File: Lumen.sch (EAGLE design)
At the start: 25 parts, among them J1 AVR_SPI_PRG_6PTH, U1 Tiny45-20-SMT, Y1 8MHZ

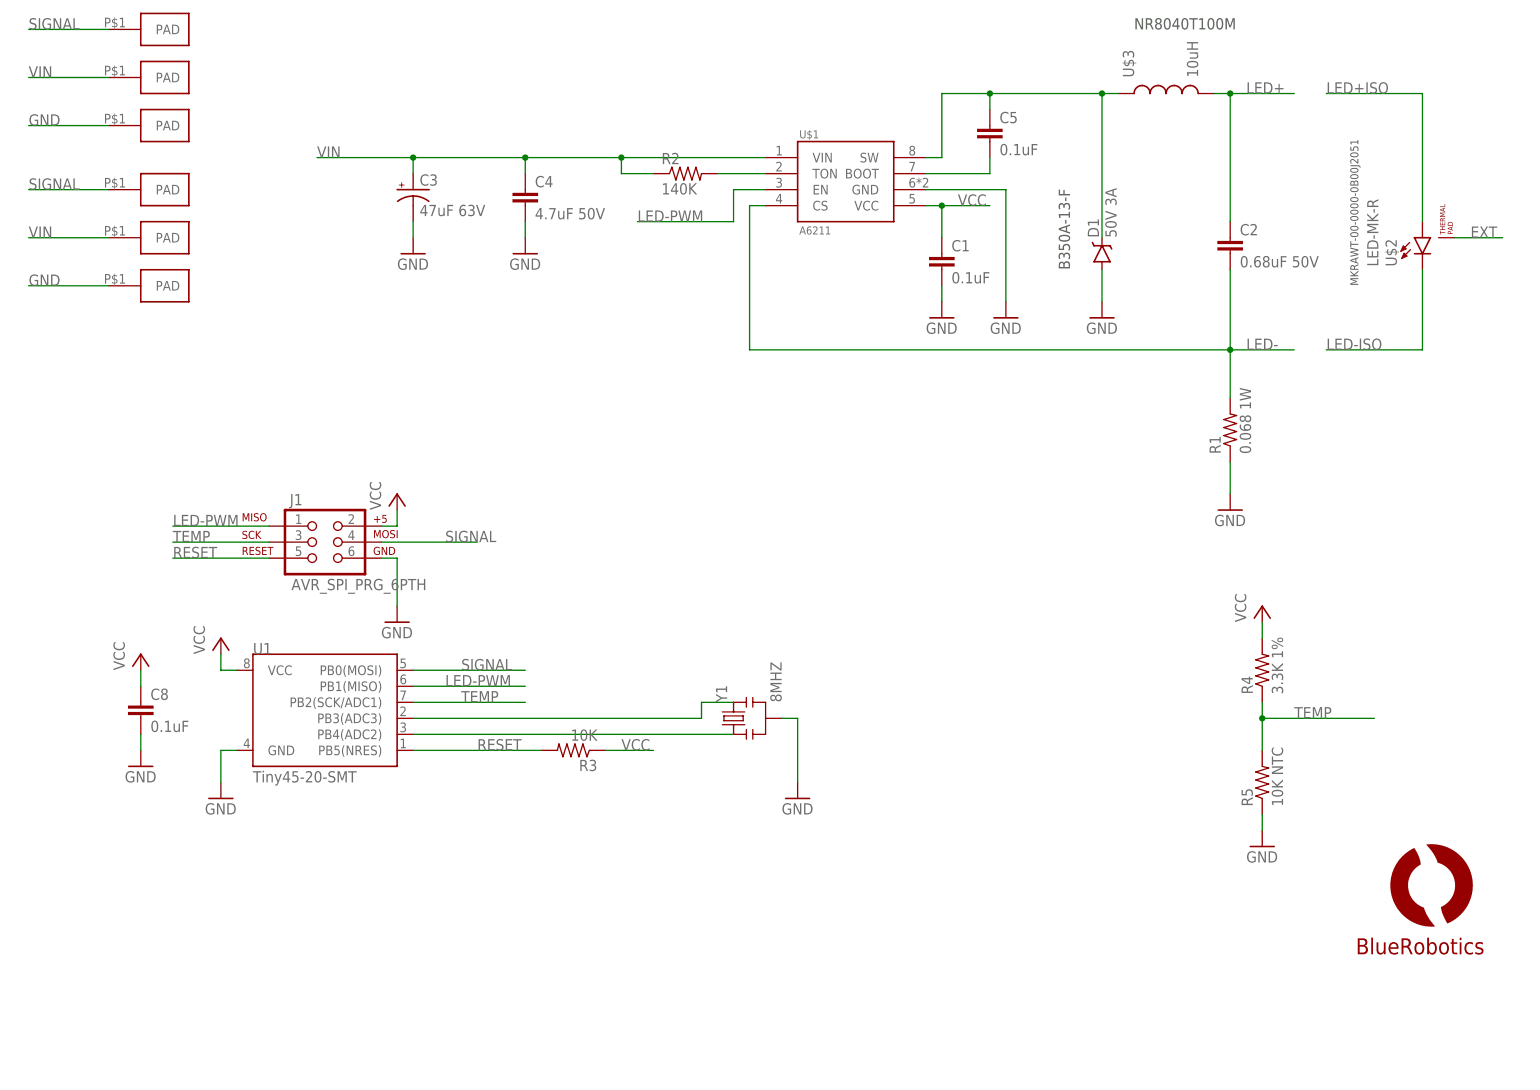
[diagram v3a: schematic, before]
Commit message: Fixed a lot of little things. Added regulator back into the design. Upgrade capacitor voltage ratings.
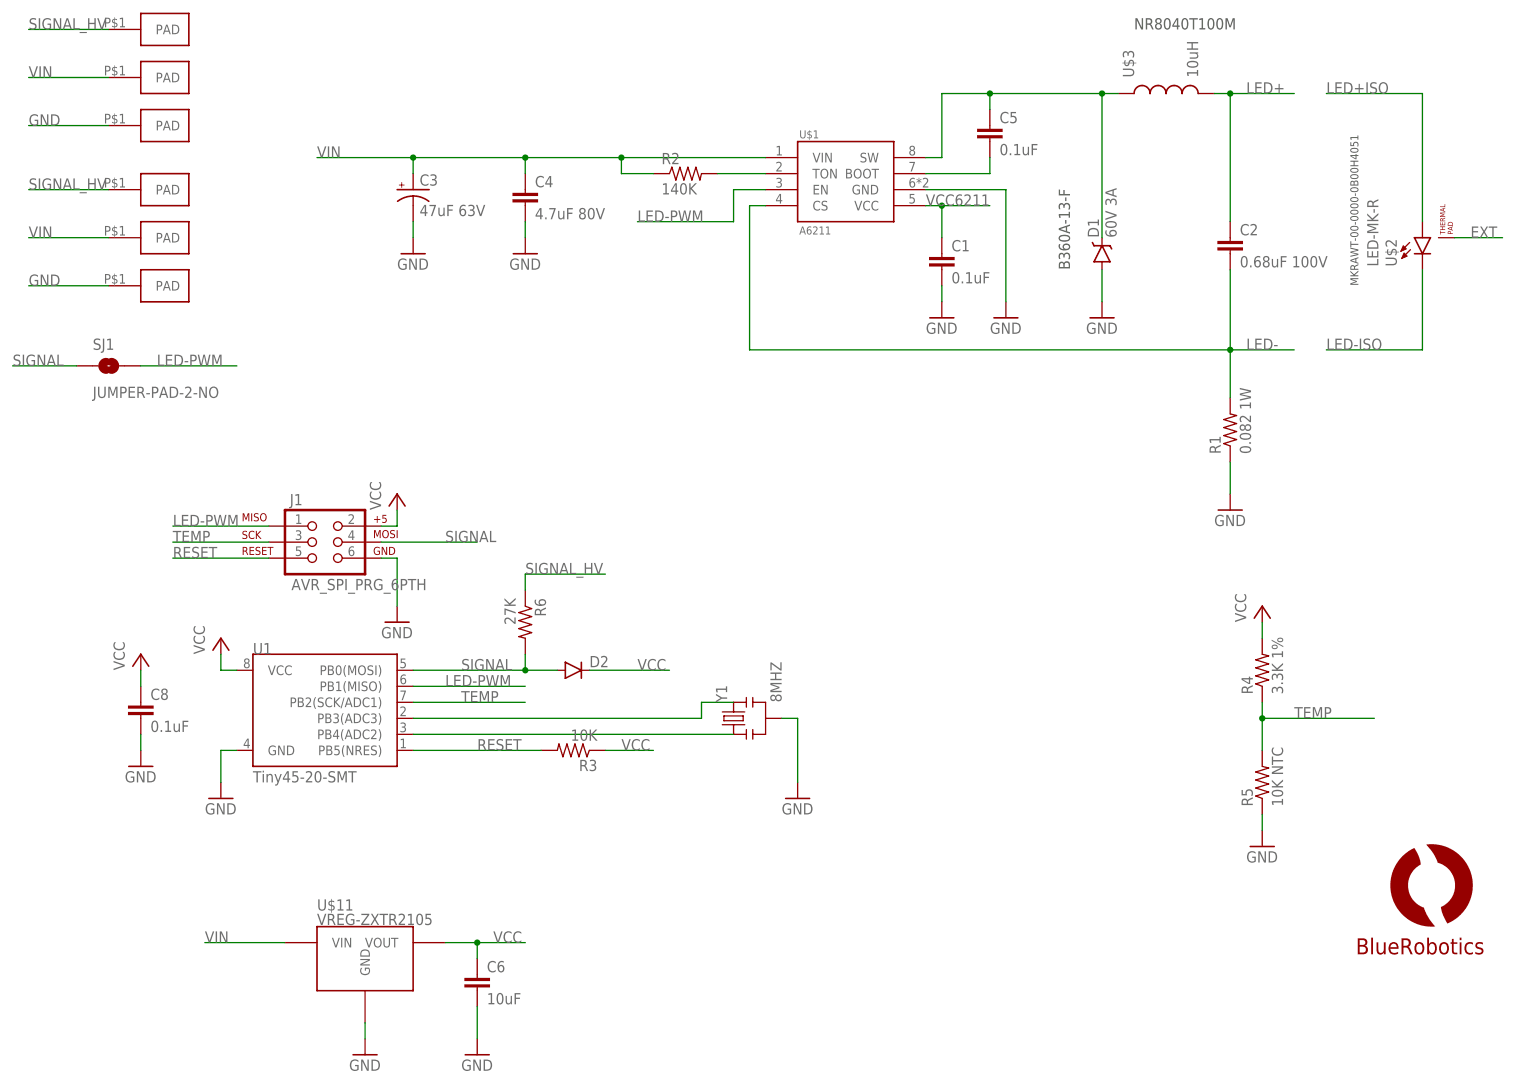
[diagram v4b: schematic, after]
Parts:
- added C6: 10uF, resistor:C-EUC0603
- added D2: (no value), SparkFun-DiscreteSemi:DIODESOD523
- added R6: 27K, resistor:R-US_R0603
- added SJ1: JUMPER-PAD-2-NO, SparkFun-Passives:JUMPER-PAD-2-NO
- added U$11: VREG-ZXTR2105, BlueRobotics-Main:VREG-ZXTR2105
- C2: value 0.68uF 50V -> 0.68uF 100V
- C4: value 4.7uF 50V -> 4.7uF 80V; device resistor:C-EUC1206 -> resistor:C-EUC1210
- D1: value 50V 3A -> 60V 3A
- R1: value 0.068 1W -> 0.082 1W; device resistor:R-US_R1210 -> resistor:R-US_R2512
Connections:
- new net SIGNAL_HV: R6.1, U$4.PAD, U$7.PAD
- new net VCC6211: C1.1, U$1.VCC
- net GND: now also C6.2, U$11.GND
- net LED-PWM: now also SJ1.2
- net SIGNAL: now also D2.A, R6.2, SJ1.1; no longer U$4.PAD, U$7.PAD
- net VCC: now also C6.1, D2.C, U$11.VOUT; no longer C1.1, U$1.VCC
- net VIN: now also U$11.VIN
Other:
- note added: "B360A-13-F"
- note added: "MKRAWT-00-0000-0B00H4051"
- note removed: "B350A-13-F"
- note removed: "MKRAWT-00-0000-0B00J2051"
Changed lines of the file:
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@@
 <part name="C3" library="SparkFun-Capacitors" deviceset="CAP_POL" device="PTH1" value="47uF 63V"/>
 <part name="U$3" library="BlueRobotics-Main" deviceset="INDUCTOR" device="8040" value="10uH"/>
-<part name="D1" library="SparkFun-DiscreteSemi" deviceset="DIODE-SCHOTTKY" device="-B340A" value="50V 3A"/>
-<part name="R1" library="resistor" deviceset="R-US_" device="R1210" value="0.068 1W"/>
-<part name="C4" library="resistor" deviceset="C-EU" device="C1206" value="4.7uF 50V"/>
-<part name="C2" library="resistor" deviceset="C-EU" device="C0805" value="0.68uF 50V"/>
+<part name="D1" library="SparkFun-DiscreteSemi" deviceset="DIODE-SCHOTTKY" device="-B340A" value="60V 3A"/>
+<part name="R1" library="resistor" deviceset="R-US_" device="R2512" value="0.082 1W"/>
+<part name="C4" library="resistor" deviceset="C-EU" device="C1210" value="4.7uF 80V"/>
+<part name="C2" library="resistor" deviceset="C-EU" device="C0805" value="0.68uF 100V"/>
 <part name="C1" library="resistor" deviceset="C-EU" device="C0603" value="0.1uF"/>
 <part name="C5" library="resistor" deviceset="C-EU" device="C0603" value="0.1uF"/>
@@
 <part name="GND8" library="supply1" deviceset="GND" device=""/>
 <part name="U$10" library="BlueRobotics-Main" deviceset="LOGO" device="BR-LOGO-MS" value="LOGOBR-LOGO-MS"/>
+<part name="U$11" library="BlueRobotics-Main" deviceset="VREG-ZXTR2105" device=""/>
+<part name="GND11" library="supply1" deviceset="GND" device=""/>
+<part name="C6" library="resistor" deviceset="C-EU" device="C0603" value="10uF"/>
+<part name="GND13" library="supply1" deviceset="GND" device=""/>
+<part name="SJ1" library="SparkFun-Passives" deviceset="JUMPER-PAD-2-NO" device=""/>
+<part name="D2" library="SparkFun-DiscreteSemi" deviceset="DIODE" device="SOD523"/>
+<part name="R6" library="resistor" deviceset="R-US_" device="R0603" value="27K"/>
 </parts>
 <sheets>
@@
 <plain>
 <text x="185.42" y="175.26" size="1.778" layer="97">NR8040T100M</text>
-<text x="175.26" y="137.16" size="1.778" layer="97" rot="R90">B350A-13-F</text>
-<text x="220.98" y="134.62" size="1.27" layer="97" rot="R90">MKRAWT-00-0000-0B00J2051</text>
+<text x="175.26" y="137.16" size="1.778" layer="97" rot="R90">B360A-13-F</text>
+<text x="220.98" y="134.62" size="1.27" layer="97" rot="R90">MKRAWT-00-0000-0B00H4051</text>
 </plain>
 <instances>
@@
 <instance part="GND8" gate="1" x="132.08" y="53.34"/>
 <instance part="U$10" gate="G$1" x="226.06" y="33.02"/>
+<instance part="U$11" gate="G$1" x="63.5" y="25.4"/>
+<instance part="GND11" gate="1" x="63.5" y="12.7"/>
+<instance part="C6" gate="G$1" x="81.28" y="25.4"/>
+<instance part="GND13" gate="1" x="81.28" y="12.7"/>
+<instance part="SJ1" gate="G$1" x="22.86" y="121.92"/>
+<instance part="D2" gate="G$1" x="96.52" y="73.66"/>
+<instance part="R6" gate="G$1" x="88.9" y="81.28" rot="R270"/>
 </instances>
 <busses>
@@
 <pinref part="Y1" gate="G$1" pin="2"/>
 <wire x1="132.08" y1="66.04" x2="129.54" y2="66.04" width="0.1524" layer="91"/>
+</segment>
+<segment>
+<pinref part="GND11" gate="1" pin="GND"/>
+<pinref part="U$11" gate="G$1" pin="GND"/>
+<wire x1="63.5" y1="15.24" x2="63.5" y2="17.78" width="0.1524" layer="91"/>
+</segment>
+<segment>
+<pinref part="GND13" gate="1" pin="GND"/>
+<pinref part="C6" gate="G$1" pin="2"/>
+<wire x1="81.28" y1="15.24" x2="81.28" y2="20.32" width="0.1524" layer="91"/>
 </segment>
 </net>
@@
 <label x="10.16" y="142.24" size="1.778" layer="95"/>
 </segment>
+<segment>
+<pinref part="U$11" gate="G$1" pin="VIN"/>
+<wire x1="50.8" y1="30.48" x2="38.1" y2="30.48" width="0.1524" layer="91"/>
+<label x="38.1" y="30.48" size="1.778" layer="95"/>
+</segment>
 </net>
 <net name="LED-PWM" class="0">
@@
 <wire x1="48.26" y1="96.52" x2="33.02" y2="96.52" width="0.1524" layer="91"/>
 <label x="33.02" y="96.52" size="1.778" layer="95"/>
+</segment>
+<segment>
+<pinref part="SJ1" gate="G$1" pin="2"/>
+<wire x1="27.94" y1="121.92" x2="43.18" y2="121.92" width="0.1524" layer="91"/>
+<label x="30.48" y="121.92" size="1.778" layer="95"/>
 </segment>
 </net>
@@
 <net name="SIGNAL" class="0">
 <segment>
-<pinref part="U$4" gate="G$1" pin="PAD"/>
-<wire x1="22.86" y1="175.26" x2="10.16" y2="175.26" width="0.1524" layer="91"/>
-<label x="10.16" y="175.26" size="1.778" layer="95"/>
-</segment>
-<segment>
-<pinref part="U$7" gate="G$1" pin="PAD"/>
-<wire x1="22.86" y1="149.86" x2="10.16" y2="149.86" width="0.1524" layer="91"/>
-<label x="10.16" y="149.86" size="1.778" layer="95"/>
-</segment>
-<segment>
 <pinref part="U1" gate="G$1" pin="PB0(MOSI)"/>
 <wire x1="71.12" y1="73.66" x2="88.9" y2="73.66" width="0.1524" layer="91"/>
 <label x="78.74" y="73.66" size="1.778" layer="95"/>
+<pinref part="D2" gate="G$1" pin="A"/>
+<pinref part="R6" gate="G$1" pin="2"/>
+<wire x1="88.9" y1="73.66" x2="93.98" y2="73.66" width="0.1524" layer="91"/>
+<wire x1="88.9" y1="76.2" x2="88.9" y2="73.66" width="0.1524" layer="91"/>
+<junction x="88.9" y="73.66"/>
 </segment>
 <segment>
@@
 <wire x1="66.04" y1="93.98" x2="81.28" y2="93.98" width="0.1524" layer="91"/>
 <label x="76.2" y="93.98" size="1.778" layer="95"/>
+</segment>
+<segment>
+<pinref part="SJ1" gate="G$1" pin="1"/>
+<wire x1="17.78" y1="121.92" x2="7.62" y2="121.92" width="0.1524" layer="91"/>
+<label x="7.62" y="121.92" size="1.778" layer="95"/>
 </segment>
 </net>
@@
 </segment>
 <segment>
-<pinref part="C1" gate="G$1" pin="1"/>
-<wire x1="154.94" y1="142.24" x2="154.94" y2="147.32" width="0.1524" layer="91"/>
-<pinref part="U$1" gate="G$1" pin="VCC"/>
-<wire x1="154.94" y1="147.32" x2="152.4" y2="147.32" width="0.1524" layer="91"/>
-<wire x1="154.94" y1="147.32" x2="162.56" y2="147.32" width="0.1524" layer="91"/>
-<junction x="154.94" y="147.32"/>
-<label x="157.48" y="147.32" size="1.778" layer="95"/>
+<pinref part="U$11" gate="G$1" pin="VOUT"/>
+<wire x1="76.2" y1="30.48" x2="81.28" y2="30.48" width="0.1524" layer="91"/>
+<label x="83.82" y="30.48" size="1.778" layer="95"/>
+<pinref part="C6" gate="G$1" pin="1"/>
+<wire x1="81.28" y1="30.48" x2="88.9" y2="30.48" width="0.1524" layer="91"/>
+<wire x1="81.28" y1="27.94" x2="81.28" y2="30.48" width="0.1524" layer="91"/>
+<junction x="81.28" y="30.48"/>
+</segment>
+<segment>
+<pinref part="D2" gate="G$1" pin="C"/>
+<wire x1="99.06" y1="73.66" x2="111.76" y2="73.66" width="0.1524" layer="91"/>
+<label x="106.68" y="73.66" size="1.778" layer="95"/>
 </segment>
 </net>
@@
 </segment>
 </net>
+<net name="VCC6211" class="0">
+<segment>
+<pinref part="C1" gate="G$1" pin="1"/>
+<wire x1="154.94" y1="142.24" x2="154.94" y2="147.32" width="0.1524" layer="91"/>
+<pinref part="U$1" gate="G$1" pin="VCC"/>
+<wire x1="154.94" y1="147.32" x2="152.4" y2="147.32" width="0.1524" layer="91"/>
+<wire x1="154.94" y1="147.32" x2="162.56" y2="147.32" width="0.1524" layer="91"/>
+<junction x="154.94" y="147.32"/>
+<label x="152.4" y="147.32" size="1.778" layer="95"/>
+</segment>
+</net>
+<net name="SIGNAL_HV" class="0">
+<segment>
+<pinref part="R6" gate="G$1" pin="1"/>
+<wire x1="88.9" y1="86.36" x2="88.9" y2="88.9" width="0.1524" layer="91"/>
+<wire x1="88.9" y1="88.9" x2="101.6" y2="88.9" width="0.1524" layer="91"/>
+<label x="88.9" y="88.9" size="1.778" layer="95"/>
+</segment>
+<segment>
+<pinref part="U$7" gate="G$1" pin="PAD"/>
+<wire x1="22.86" y1="149.86" x2="10.16" y2="149.86" width="0.1524" layer="91"/>
+<label x="10.16" y="149.86" size="1.778" layer="95"/>
+</segment>
+<segment>
+<pinref part="U$4" gate="G$1" pin="PAD"/>
+<wire x1="22.86" y1="175.26" x2="10.16" y2="175.26" width="0.1524" layer="91"/>
+<label x="10.16" y="175.26" size="1.778" layer="95"/>
+</segment>
+</net>

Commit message: Fixed some layout issues per John's suggestion. Added pads for a snubber that will probably not be populated.
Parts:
- added C7: NP, resistor:C-EUC0603
- added R7: NP, resistor:R-US_R0603
- D1: device SparkFun-DiscreteSemi:DIODE-SCHOTTKY-B340A -> BlueRobotics-Main:DIODE-SCHOTTKYSMA
- D2: value (none) -> BAT54; device SparkFun-DiscreteSemi:DIODESOD523 -> BlueRobotics-Main:DIODE-SCHOTTKYSOD523
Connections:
- new net N$2: C7.2, R7.1
- net GND: now also R7.2
- net N$5: now also C7.1
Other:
- note added: "Snubber"
- moved on the sheet: C1, C3, C4, C5, R2, U$1

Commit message: More updates based on J.N. comments. Ready to order I believe.
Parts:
- R7: device resistor:R-US_R0603 -> resistor:R-US_R1206
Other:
- moved on the sheet: R4, R5
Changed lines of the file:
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@@
 <part name="U1" library="SparkFun-DigitalIC" deviceset="ATTINY45" device="TINY45-20-SMT" value="Tiny45-20-SMT"/>
 <part name="U$1" library="BlueRobotics-Main" deviceset="A6211" device=""/>
-<part name="FRAME1" library="BlueRobotics-Main" deviceset="FRAME-BLUEROBOTICS" device="" value="µC and LED Driver"/>
+<part name="FRAME1" library="BlueRobotics-Main" deviceset="FRAME-BLUEROBOTICS" device="" value="Microcontroller and LED Driver"/>
 <part name="U$2" library="BlueRobotics-Main" deviceset="LED-MK-R" device=""/>
 <part name="C3" library="SparkFun-Capacitors" deviceset="CAP_POL" device="PTH1" value="47uF 63V"/>
@@
 <part name="GND14" library="supply1" deviceset="GND" device=""/>
 <part name="C7" library="resistor" deviceset="C-EU" device="C0603" value="NP"/>
-<part name="R7" library="resistor" deviceset="R-US_" device="R0603" value="NP"/>
+<part name="R7" library="resistor" deviceset="R-US_" device="R1206" value="NP"/>
 </parts>
 <sheets>
@@
 <instance part="U$8" gate="G$1" x="33.02" y="142.24"/>
 <instance part="U$9" gate="G$1" x="33.02" y="134.62"/>
-<instance part="R4" gate="G$1" x="205.74" y="73.66" rot="R90"/>
-<instance part="R5" gate="G$1" x="205.74" y="55.88" rot="R90"/>
-<instance part="GND9" gate="1" x="205.74" y="45.72"/>
-<instance part="P+1" gate="VCC" x="205.74" y="83.82"/>
+<instance part="R4" gate="G$1" x="165.1" y="73.66" rot="R90"/>
+<instance part="R5" gate="G$1" x="165.1" y="55.88" rot="R90"/>
+<instance part="GND9" gate="1" x="165.1" y="45.72"/>
+<instance part="P+1" gate="VCC" x="165.1" y="83.82"/>
 <instance part="P+2" gate="VCC" x="40.64" y="78.74"/>
 <instance part="P+3" gate="VCC" x="68.58" y="101.6"/>
@@
 <pinref part="GND9" gate="1" pin="GND"/>
 <pinref part="R5" gate="G$1" pin="1"/>
-<wire x1="205.74" y1="48.26" x2="205.74" y2="50.8" width="0.1524" layer="91"/>
+<wire x1="165.1" y1="48.26" x2="165.1" y2="50.8" width="0.1524" layer="91"/>
 </segment>
 <segment>
@@
 <pinref part="R4" gate="G$1" pin="2"/>
 <pinref part="P+1" gate="VCC" pin="VCC"/>
-<wire x1="205.74" y1="78.74" x2="205.74" y2="81.28" width="0.1524" layer="91"/>
+<wire x1="165.1" y1="78.74" x2="165.1" y2="81.28" width="0.1524" layer="91"/>
 </segment>
 <segment>
@@
 <pinref part="R5" gate="G$1" pin="2"/>
 <pinref part="R4" gate="G$1" pin="1"/>
-<wire x1="205.74" y1="60.96" x2="205.74" y2="66.04" width="0.1524" layer="91"/>
-<wire x1="205.74" y1="66.04" x2="205.74" y2="68.58" width="0.1524" layer="91"/>
-<wire x1="205.74" y1="66.04" x2="223.52" y2="66.04" width="0.1524" layer="91"/>
-<junction x="205.74" y="66.04"/>
-<label x="210.82" y="66.04" size="1.778" layer="95"/>
-</segment>
-</net>
+<wire x1="165.1" y1="60.96" x2="165.1" y2="66.04" width="0.1524" layer="91"/>
+<wire x1="165.1" y1="66.04" x2="165.1" y2="68.58" width="0.1524" layer="91"/>
+<wire x1="165.1" y1="66.04" x2="182.88" y2="66.04" width="0.1524" layer="91"/>
+<junction x="165.1" y="66.04"/>
+<label x="170.18" y="66.04" size="1.778" layer="95"/>
+</segment>
+</net>

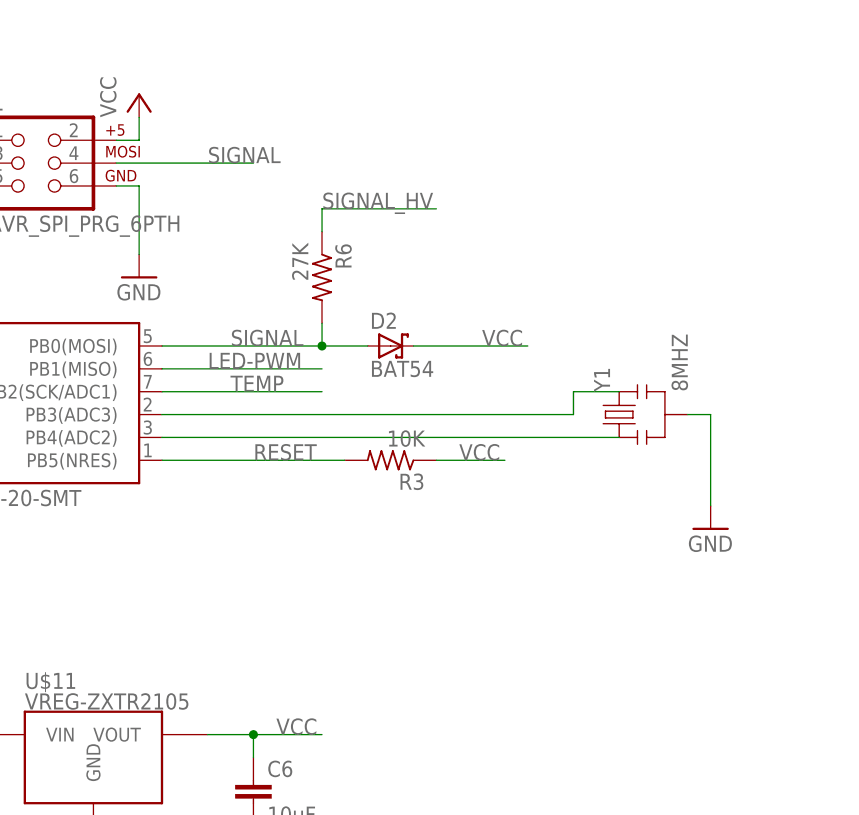
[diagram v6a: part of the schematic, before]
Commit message: Adjusted signal pull-down for 3.3V compatibility.
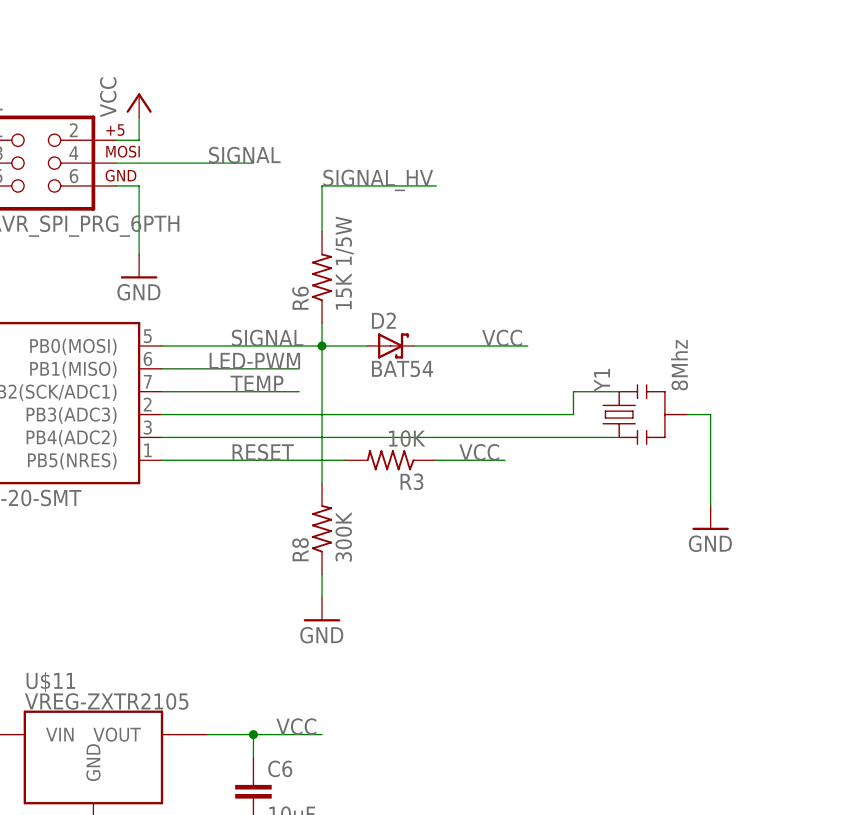
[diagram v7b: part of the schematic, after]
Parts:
- added R8: 300K, resistor:R-US_R0402
- R6: value 27K -> 15K 1/5W; device resistor:R-US_R0603 -> resistor:R-US_R0402
- U$10: value LOGOBR-LOGO-MS -> LOGOBR-LOGO-MS-COPPER; device BlueRobotics-Main:LOGOBR-LOGO-MS -> BlueRobotics-Main:LOGOBR-LOGO-MS-COPPER
- Y1: value 8MHZ -> 8Mhz; device SparkFun-FreqCtrl:RESONATOR16MHZ -> SparkFun:RESONATORSMD
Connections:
- net GND: now also R8.1
- net SIGNAL: now also R6.1, R8.2; no longer R6.2
- net SIGNAL_HV: now also R6.2; no longer R6.1
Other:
- moved on the sheet: R6
